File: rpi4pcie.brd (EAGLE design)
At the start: 8 x 10 mm, 88 parts

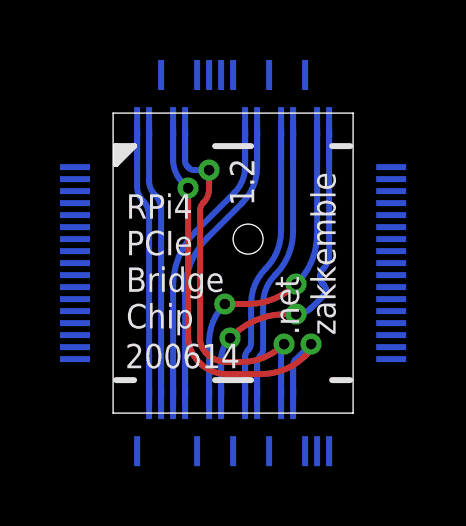
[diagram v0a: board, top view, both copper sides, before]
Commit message: Remove extra pads from PCB for fab
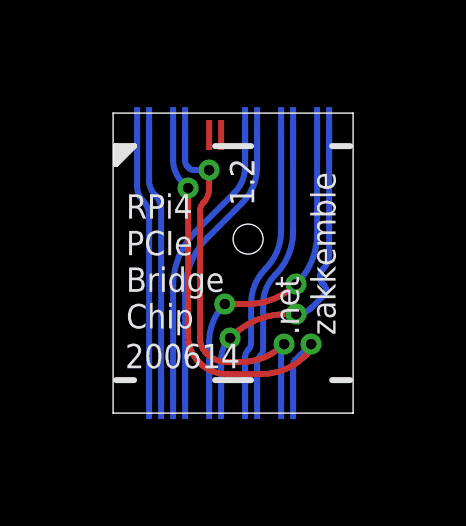
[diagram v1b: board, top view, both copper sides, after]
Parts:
- removed PAD1, PAD10, PAD11, PAD12, PAD13, PAD14, PAD15, PAD16, PAD17, PAD18, PAD2, PAD23, PAD26, PAD29, PAD3, PAD32, PAD33, PAD34, PAD35, PAD36, PAD37, PAD38, PAD39, PAD4, PAD40, PAD41, PAD42, PAD43, PAD44, PAD45, PAD46, PAD47, PAD48, PAD49, PAD5, PAD50, PAD51, PAD54, PAD57, PAD6, PAD60, PAD63, PAD66, PAD7, PAD8, PAD9: PADQFN-0.4, zak:PAD-QFN-0.4
- moved PAD61 2.00 mm to (5.60, 11.3), flipped to the top
- moved PAD62 2.00 mm to (5.20, 11.3), flipped to the top
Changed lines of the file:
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@@
 <?xml version="1.0" encoding="utf-8"?>
 <!DOCTYPE eagle SYSTEM "eagle.dtd">
-<eagle version="9.4.1">
+<eagle version="9.6.1">
 <drawing>
 <settings>
-<setting alwaysvectorfont="yes"/>
+<setting alwaysvectorfont="no"/>
 <setting keepoldvectorfont="yes"/>
 <setting verticaltext="up"/>
@@
 </autorouter>
 <elements>
-<element name="PAD1" library="zak" package="PAD-QFN-0.4" value="PADQFN-0.4" x="0.73" y="10.2" smashed="yes" rot="MR90"/>
-<element name="PAD2" library="zak" package="PAD-QFN-0.4" value="PADQFN-0.4" x="0.73" y="9.8" smashed="yes" rot="MR90"/>
-<element name="PAD3" library="zak" package="PAD-QFN-0.4" value="PADQFN-0.4" x="0.73" y="9.4" smashed="yes" rot="MR90"/>
-<element name="PAD4" library="zak" package="PAD-QFN-0.4" value="PADQFN-0.4" x="0.73" y="9" smashed="yes" rot="MR90"/>
-<element name="PAD5" library="zak" package="PAD-QFN-0.4" value="PADQFN-0.4" x="0.73" y="8.6" smashed="yes" rot="MR90"/>
-<element name="PAD6" library="zak" package="PAD-QFN-0.4" value="PADQFN-0.4" x="0.73" y="8.2" smashed="yes" rot="MR90"/>
-<element name="PAD7" library="zak" package="PAD-QFN-0.4" value="PADQFN-0.4" x="0.73" y="7.8" smashed="yes" rot="MR90"/>
-<element name="PAD8" library="zak" package="PAD-QFN-0.4" value="PADQFN-0.4" x="0.73" y="7.4" smashed="yes" rot="MR90"/>
-<element name="PAD9" library="zak" package="PAD-QFN-0.4" value="PADQFN-0.4" x="0.73" y="7" smashed="yes" rot="MR90"/>
-<element name="PAD10" library="zak" package="PAD-QFN-0.4" value="PADQFN-0.4" x="0.73" y="6.6" smashed="yes" rot="MR90"/>
-<element name="PAD11" library="zak" package="PAD-QFN-0.4" value="PADQFN-0.4" x="0.73" y="6.2" smashed="yes" rot="MR90"/>
-<element name="PAD12" library="zak" package="PAD-QFN-0.4" value="PADQFN-0.4" x="0.73" y="5.8" smashed="yes" rot="MR90"/>
-<element name="PAD13" library="zak" package="PAD-QFN-0.4" value="PADQFN-0.4" x="0.73" y="5.4" smashed="yes" rot="MR90"/>
-<element name="PAD14" library="zak" package="PAD-QFN-0.4" value="PADQFN-0.4" x="0.73" y="5" smashed="yes" rot="MR90"/>
-<element name="PAD15" library="zak" package="PAD-QFN-0.4" value="PADQFN-0.4" x="0.73" y="4.6" smashed="yes" rot="MR90"/>
-<element name="PAD16" library="zak" package="PAD-QFN-0.4" value="PADQFN-0.4" x="0.73" y="4.2" smashed="yes" rot="MR90"/>
-<element name="PAD17" library="zak" package="PAD-QFN-0.4" value="PADQFN-0.4" x="0.73" y="3.8" smashed="yes" rot="MR90"/>
-<element name="PAD18" library="zak" package="PAD-QFN-0.4" value="PADQFN-0.4" x="2.8" y="0.73" smashed="yes" rot="MR0"/>
 <element name="PAD19" library="zak" package="PAD-QFN-0.4" value="PADQFN-0.4" x="3.2" y="3.1" smashed="yes" rot="MR0"/>
 <element name="PAD20" library="zak" package="PAD-QFN-0.4" value="PADQFN-0.4" x="3.6" y="3.1" smashed="yes" rot="MR0"/>
 <element name="PAD21" library="zak" package="PAD-QFN-0.4" value="PADQFN-0.4" x="4" y="3.1" smashed="yes" rot="MR0"/>
 <element name="PAD22" library="zak" package="PAD-QFN-0.4" value="PADQFN-0.4" x="4.4" y="3.1" smashed="yes" rot="MR0"/>
-<element name="PAD23" library="zak" package="PAD-QFN-0.4" value="PADQFN-0.4" x="4.8" y="0.73" smashed="yes" rot="MR0"/>
 <element name="PAD24" library="zak" package="PAD-QFN-0.4" value="PADQFN-0.4" x="5.2" y="3.1" smashed="yes" rot="MR0"/>
 <element name="PAD25" library="zak" package="PAD-QFN-0.4" value="PADQFN-0.4" x="5.6" y="3.1" smashed="yes" rot="MR0"/>
-<element name="PAD26" library="zak" package="PAD-QFN-0.4" value="PADQFN-0.4" x="6" y="0.73" smashed="yes" rot="MR0"/>
 <element name="PAD27" library="zak" package="PAD-QFN-0.4" value="PADQFN-0.4" x="6.4" y="3.1" smashed="yes" rot="MR0"/>
 <element name="PAD28" library="zak" package="PAD-QFN-0.4" value="PADQFN-0.4" x="6.8" y="3.1" smashed="yes" rot="MR0"/>
-<element name="PAD29" library="zak" package="PAD-QFN-0.4" value="PADQFN-0.4" x="7.2" y="0.73" smashed="yes" rot="MR0"/>
 <element name="PAD30" library="zak" package="PAD-QFN-0.4" value="PADQFN-0.4" x="7.6" y="3.1" smashed="yes" rot="MR0"/>
 <element name="PAD31" library="zak" package="PAD-QFN-0.4" value="PADQFN-0.4" x="8" y="3.1" smashed="yes" rot="MR0"/>
-<element name="PAD32" library="zak" package="PAD-QFN-0.4" value="PADQFN-0.4" x="8.4" y="0.73" smashed="yes" rot="MR0"/>
-<element name="PAD33" library="zak" package="PAD-QFN-0.4" value="PADQFN-0.4" x="8.8" y="0.73" smashed="yes" rot="MR0"/>
-<element name="PAD34" library="zak" package="PAD-QFN-0.4" value="PADQFN-0.4" x="9.2" y="0.73" smashed="yes" rot="MR0"/>
-<element name="PAD35" library="zak" package="PAD-QFN-0.4" value="PADQFN-0.4" x="11.27" y="3.8" smashed="yes" rot="MR90"/>
-<element name="PAD36" library="zak" package="PAD-QFN-0.4" value="PADQFN-0.4" x="11.27" y="4.2" smashed="yes" rot="MR90"/>
-<element name="PAD37" library="zak" package="PAD-QFN-0.4" value="PADQFN-0.4" x="11.27" y="4.6" smashed="yes" rot="MR90"/>
-<element name="PAD38" library="zak" package="PAD-QFN-0.4" value="PADQFN-0.4" x="11.27" y="5" smashed="yes" rot="MR90"/>
-<element name="PAD39" library="zak" package="PAD-QFN-0.4" value="PADQFN-0.4" x="11.27" y="5.4" smashed="yes" rot="MR90"/>
-<element name="PAD40" library="zak" package="PAD-QFN-0.4" value="PADQFN-0.4" x="11.27" y="5.8" smashed="yes" rot="MR90"/>
-<element name="PAD41" library="zak" package="PAD-QFN-0.4" value="PADQFN-0.4" x="11.27" y="6.2" smashed="yes" rot="MR90"/>
-<element name="PAD42" library="zak" package="PAD-QFN-0.4" value="PADQFN-0.4" x="11.27" y="6.6" smashed="yes" rot="MR90"/>
-<element name="PAD43" library="zak" package="PAD-QFN-0.4" value="PADQFN-0.4" x="11.27" y="7" smashed="yes" rot="MR90"/>
-<element name="PAD44" library="zak" package="PAD-QFN-0.4" value="PADQFN-0.4" x="11.27" y="7.4" smashed="yes" rot="MR90"/>
-<element name="PAD45" library="zak" package="PAD-QFN-0.4" value="PADQFN-0.4" x="11.27" y="7.8" smashed="yes" rot="MR90"/>
-<element name="PAD46" library="zak" package="PAD-QFN-0.4" value="PADQFN-0.4" x="11.27" y="8.2" smashed="yes" rot="MR90"/>
-<element name="PAD47" library="zak" package="PAD-QFN-0.4" value="PADQFN-0.4" x="11.27" y="8.6" smashed="yes" rot="MR90"/>
-<element name="PAD48" library="zak" package="PAD-QFN-0.4" value="PADQFN-0.4" x="11.27" y="9" smashed="yes" rot="MR90"/>
-<element name="PAD49" library="zak" package="PAD-QFN-0.4" value="PADQFN-0.4" x="11.27" y="9.4" smashed="yes" rot="MR90"/>
-<element name="PAD50" library="zak" package="PAD-QFN-0.4" value="PADQFN-0.4" x="11.27" y="9.8" smashed="yes" rot="MR90"/>
-<element name="PAD51" library="zak" package="PAD-QFN-0.4" value="PADQFN-0.4" x="11.27" y="10.2" smashed="yes" rot="MR90"/>
 <element name="PAD52" library="zak" package="PAD-QFN-0.4" value="PADQFN-0.4" x="9.2" y="10.9" smashed="yes" rot="MR0"/>
 <element name="PAD53" library="zak" package="PAD-QFN-0.4" value="PADQFN-0.4" x="8.8" y="10.9" smashed="yes" rot="MR0"/>
-<element name="PAD54" library="zak" package="PAD-QFN-0.4" value="PADQFN-0.4" x="8.4" y="13.27" smashed="yes" rot="MR0"/>
 <element name="PAD55" library="zak" package="PAD-QFN-0.4" value="PADQFN-0.4" x="8" y="10.9" smashed="yes" rot="MR0"/>
 <element name="PAD56" library="zak" package="PAD-QFN-0.4" value="PADQFN-0.4" x="7.6" y="10.9" smashed="yes" rot="MR0"/>
-<element name="PAD57" library="zak" package="PAD-QFN-0.4" value="PADQFN-0.4" x="7.2" y="13.27" smashed="yes" rot="MR0"/>
 <element name="PAD58" library="zak" package="PAD-QFN-0.4" value="PADQFN-0.4" x="6.8" y="10.9" smashed="yes" rot="MR0"/>
 <element name="PAD59" library="zak" package="PAD-QFN-0.4" value="PADQFN-0.4" x="6.4" y="10.9" smashed="yes" rot="MR0"/>
-<element name="PAD60" library="zak" package="PAD-QFN-0.4" value="PADQFN-0.4" x="6" y="13.27" smashed="yes" rot="MR0"/>
-<element name="PAD61" library="zak" package="PAD-QFN-0.4" value="PADQFN-0.4" x="5.6" y="13.27" smashed="yes" rot="MR0"/>
-<element name="PAD62" library="zak" package="PAD-QFN-0.4" value="PADQFN-0.4" x="5.2" y="13.27" smashed="yes" rot="MR0"/>
-<element name="PAD63" library="zak" package="PAD-QFN-0.4" value="PADQFN-0.4" x="4.8" y="13.27" smashed="yes" rot="MR0"/>
+<element name="PAD61" library="zak" package="PAD-QFN-0.4" value="PADQFN-0.4" x="5.6" y="11.27" smashed="yes"/>
+<element name="PAD62" library="zak" package="PAD-QFN-0.4" value="PADQFN-0.4" x="5.2" y="11.27" smashed="yes"/>
 <element name="PAD64" library="zak" package="PAD-QFN-0.4" value="PADQFN-0.4" x="4.4" y="10.9" smashed="yes" rot="MR0"/>
 <element name="PAD65" library="zak" package="PAD-QFN-0.4" value="PADQFN-0.4" x="4" y="10.9" smashed="yes" rot="MR0"/>
-<element name="PAD66" library="zak" package="PAD-QFN-0.4" value="PADQFN-0.4" x="3.6" y="13.27" smashed="yes" rot="MR0"/>
 <element name="PAD67" library="zak" package="PAD-QFN-0.4" value="PADQFN-0.4" x="3.2" y="10.9" smashed="yes" rot="MR0"/>
 <element name="PAD68" library="zak" package="PAD-QFN-0.4" value="PADQFN-0.4" x="2.8" y="10.9" smashed="yes" rot="MR0"/>
